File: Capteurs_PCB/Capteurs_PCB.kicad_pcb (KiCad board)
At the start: 2 copper layers, 51 x 70 mm, 55 parts, among them J1 Conn_01x04, J101 Conn_01x03, J103 Conn_02x20_Odd_Even, J104 Conn_ST_STDC14, J2 Conn_01x03, J3 Alim_Prop2, J4 Conn_01x02, J5 Alim_Prop1, J6 Conn_01x03, J7 Conn_01x03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

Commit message: Update Capteurs_PCB.kicad_pcb
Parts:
- added U2: ~, Custom:Regulator, F.Cu at (72.7, 65.8)
- added U401: ~, Custom:Regulator, F.Cu at (79.8, 65.8)
- added U402: ~, Custom:Regulator, F.Cu at (86.9, 65.8)
- added U6: 32350268, Custom:Pressure_Captor_Custom, F.Cu at (73.3, 78.0)

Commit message: Début de routage
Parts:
- removed J3: Alim_Prop2, Connector_Hirose:Hirose_DF13-02P-1.25DSA_1x02_P1.25mm_Vertical
- removed J5: Alim_Prop1, Connector_Hirose:Hirose_DF13-02P-1.25DSA_1x02_P1.25mm_Vertical
- removed the U2 at (127.8, 110.5)
- removed the U401 at (127.8, 98.5)
- removed the U402 at (127.8, 87.5)
- removed the U6 at (126.0, 60.1)
- J1: footprint Connector_PinSocket_2.54mm:PinSocket_1x04_P2.54mm_Vertical -> Connector_JST:JST_XH_B4B-XH-A_1x04_P2.50mm_Vertical
- J101, J6, J7: footprint Connector_PinHeader_2.54mm:PinHeader_1x03_P2.54mm_Vertical -> Connector_JST:JST_XH_B3B-XH-A_1x03_P2.50mm_Vertical
- J2: footprint Connector_PinSocket_2.54mm:PinSocket_1x03_P2.54mm_Vertical -> Connector_JST:JST_XH_B3B-XH-A_1x03_P2.50mm_Vertical
- J4: footprint Connector_PinHeader_2.54mm:PinHeader_1x02_P2.54mm_Vertical -> Connector_AMASS:AMASS_XT60-M_1x02_P7.20mm_Vertical
- moved U402 62.6 mm to (148.6, 76.5)
- moved U401 62.1 mm to (125.0, 108.5), turned to -90 degrees
- moved U6 60.5 mm to (131.7, 62.2)
- moved U2 55.1 mm to (123.3, 87.7), turned to -90 degrees
- moved C406 41.2 mm to (151.5, 67.5)
- moved D401 36.9 mm to (154.8, 74.9), turned to 180 degrees
- moved R407 35.8 mm to (154.6, 72.7), turned to 180 degrees
- moved R2 30.0 mm to (154.0, 81.0), turned to 180 degrees
- moved R1 28.0 mm to (154.0, 83.5), turned to 0 degrees
- moved C8 25.2 mm to (133.1, 93.5), turned to 90 degrees
- moved R4 24.6 mm to (116.1, 92.1)
- moved C405 23.4 mm to (154.0, 78.5)
- moved R403 22.4 mm to (120.3, 114.4)
- moved D402 22.1 mm to (127.6, 115.4)
- moved C403 22.1 mm to (133.3, 84.4), turned to -90 degrees
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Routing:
- net +3.3V: track 0.02 -> 48.9 mm, vias 0 -> 2
- net +BATT: track 0.00 -> 48.1 mm
- net +5V: track 0.00 -> 35.6 mm
- net +7.5V: track 0.00 -> 20.3 mm
- net /VDD_SER: track 0.00 -> 20.0 mm
- net /DATA1: track 0.00 -> 19.9 mm
- net /INT1: track 0.00 -> 14.1 mm
- net /INT2: track 0.00 -> 13.9 mm
- net /DATA2: track 0.00 -> 8.31 mm
- net +3.3VA: track 0.00 -> 7.84 mm
- net Net-(U401-FB): track 0.00 -> 4.88 mm
- net Net-(U402-FB): track 0.00 -> 4.72 mm
- net Net-(U401-Vcc): track 0.00 -> 3.29 mm
- net /NRST: track 0.00 -> 2.50 mm
- net Net-(D401-A): track 0.00 -> 2.42 mm
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- added copper zone on B.Cu, net GND
- added copper zone on F.Cu, net GND
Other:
- board size 51 x 70 mm -> 64 x 70 mm

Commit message: Routage
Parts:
- moved R408 32.2 mm to (122.6, 83.9), turned to -90 degrees
- moved C402 31.8 mm to (117.5, 86.2), turned to -90 degrees
- moved D402 31.7 mm to (124.2, 83.9), turned to -90 degrees
- moved R403 31.6 mm to (131.5, 84.9), turned to 90 degrees
- moved R402 30.4 mm to (129.4, 84.9), turned to -90 degrees
- moved C401 29.7 mm to (127.5, 84.9), turned to -90 degrees
- moved R401 29.3 mm to (133.9, 87.3), turned to -90 degrees
- moved C404 18.7 mm to (117.5, 95.6), turned to 90 degrees
- moved U401 17.8 mm to (126.8, 90.8), turned to 90 degrees
- moved R4 17.4 mm to (112.7, 109.2)
- moved C403 17.4 mm to (129.9, 101.5)
- moved C8 17.4 mm to (129.7, 110.5)
- moved C9 17.4 mm to (118.3, 110.8)
- moved D403 17.4 mm to (121.0, 110.6)
- moved R3 17.4 mm to (114.6, 110.8)
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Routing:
- net +3.3V: track 48.9 -> 127.4 mm, vias 2 -> 4
- net +BATT: track 48.1 -> 105.5 mm
- net /NRST: track 2.50 -> 48.6 mm, vias 0 -> 2
- net /ST_RX: track 0.00 -> 29.5 mm
- net +3V3: track 0.00 -> 24.7 mm
- net /SS: track 0.00 -> 24.4 mm, vias 0 -> 2
- net /MISO: track 0.00 -> 21.2 mm, vias 0 -> 2
- net /DATA1: track 19.9 -> 0.69 mm
- net +5V: track 35.6 -> 49.8 mm
- net /INT2: track 13.9 -> 0.14 mm
- net /SCLK: track 0.00 -> 10.6 mm, vias 0 -> 2
- net /MOSI: track 0.00 -> 10.5 mm
- net /SWO: track 0.00 -> 10.3 mm
- net /SWCLK: track 0.00 -> 8.96 mm
- net /SWDIO: track 0.00 -> 8.76 mm
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
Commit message: Le routage continue
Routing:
- net +5V: track 49.8 -> 119.1 mm
- net /RPI_UART_TX: track 0.00 -> 63.6 mm, vias 0 -> 2
- net +3.3V: track 127.4 -> 163.4 mm, vias 4 -> 5
- net /SigProp1: track 0.00 -> 35.8 mm, vias 0 -> 2
- net /SigProp2: track 0.00 -> 29.0 mm, vias 0 -> 2
- net /DATA1: track 0.69 -> 28.6 mm, vias 0 -> 2
- net /ST_TX: track 0.00 -> 13.2 mm, vias 0 -> 2

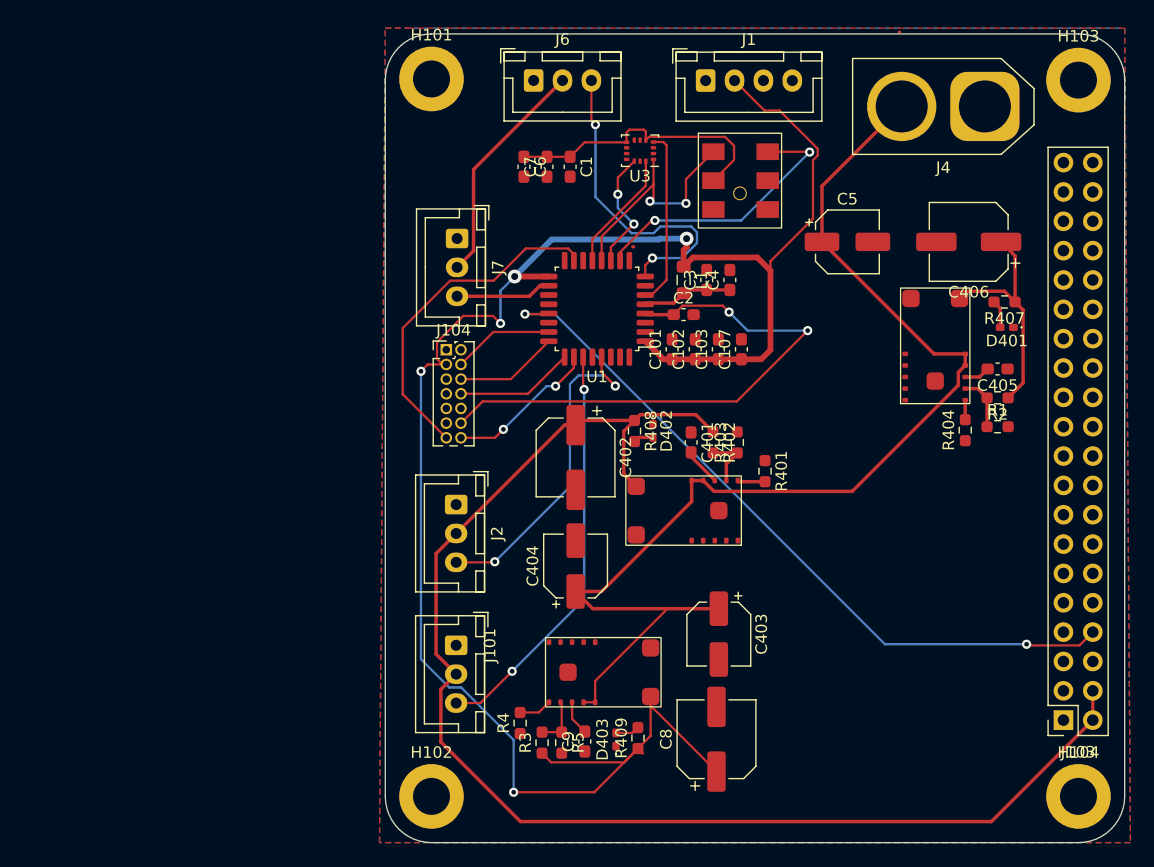
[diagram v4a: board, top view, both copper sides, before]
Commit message: Avancement PCB mais encore des problèmes
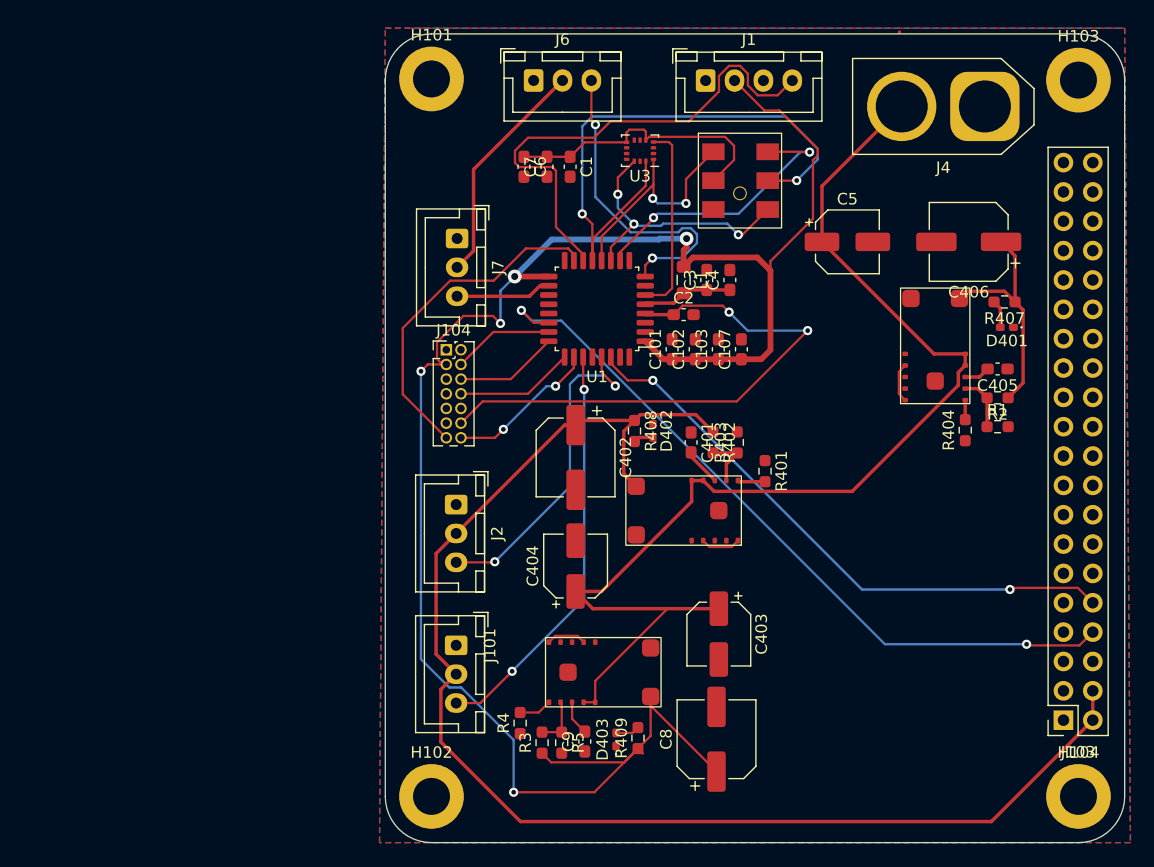
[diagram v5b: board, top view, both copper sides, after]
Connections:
- U1 pad 14: unconnected-(U1-PB0-Pad14) -> /Sig_LED
- U1 pad 20: /Sig_LED -> unconnected-(U1-PA10-Pad20)
- U1 pad 21: /RPI_UART_TX -> unconnected-(U1-PA11-Pad21)
- U1 pad 22: /RPI_UART_RX -> /RPI_UART_TX
- U1 pad 30: unconnected-(U1-PB7-Pad30) -> /RPI_UART_RX
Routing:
- net /RPI_UART_RX: track 0.00 -> 51.0 mm, vias 0 -> 2
- net /Sig_LED: track 0.00 -> 43.7 mm
- net /MOSI: track 10.5 -> 50.4 mm, vias 0 -> 2
- net /SCLK: track 10.6 -> 23.6 mm, vias 2 -> 3
- net Net-(U402-En): track 0.00 -> 3.46 mm
- net Net-(U2-En): track 0.00 -> 3.46 mm
- net Net-(U401-En): track 0.00 -> 3.46 mm
- net /INT1: track 15.3 -> 16.7 mm
- net /RPI_UART_TX: track 63.6 -> 64.8 mm
- net /MISO: track 21.2 -> 20.4 mm

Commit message: Derniers changements mais encore des erreurs
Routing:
- net /SCLK: track 23.6 -> 26.8 mm

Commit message: Modification du PCB
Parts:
- R1: value 52.2k -> 56k
- R403: value 80.4k -> 82k
- moved J104 0.16 mm to (106.4, 76.8)
- turned C101 to -90 degrees
- turned C102 to -90 degrees
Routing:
- net /INT2: track 0.14 -> 38.6 mm, vias 0 -> 2
- net Net-(U401-En): track 3.46 -> 15.9 mm
- net GND: track 0.00 -> 8.48 mm, vias 0 -> 1
- net /MOSI: track 50.4 -> 55.7 mm
- net +3.3V: track 163.2 -> 161.7 mm
- net /INT1: track 16.7 -> 17.4 mm

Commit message: PCB
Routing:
- net /DATA1: track 28.3 -> 27.7 mm
- net +3.3V: track 161.7 -> 161.1 mm
